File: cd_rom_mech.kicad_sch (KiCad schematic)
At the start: 182 parts, among them IC101 CXA1081, IC102 CXA1082BQ, IC107 RC4558, IC108 BA6290A, IC109 BA6290A, IC201 LC7881M, IC202 RC4558, IC203 RC4558, IC304 No Markings, Q608 BR 29

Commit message: Add more capacitor values, rearrange some schematics.
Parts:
- C105: value ~ -> 3.3uF 63V
- C105: value ? -> 22uF 6V
- C105: value ~ -> 22uF 6V
- C105: value ~ -> 470nF 25V
- C127: value ? -> 4.7uF 6V
- C138: value ? -> 470nF 25V
- C138: value 4.5nF -> 4.7nF
- VR101, VR103, VR104: value ~ -> 22K
- VR102: value ~ -> 15K
- VR105: value ~ -> 500
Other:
- moved on the sheet: C105, C127, C138, R105

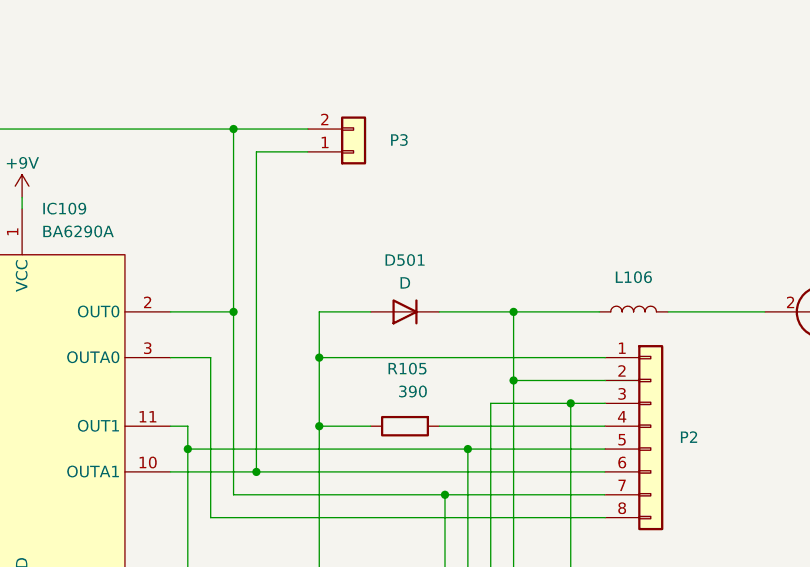
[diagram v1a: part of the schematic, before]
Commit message: Add markings for SMD Ds and Qs.
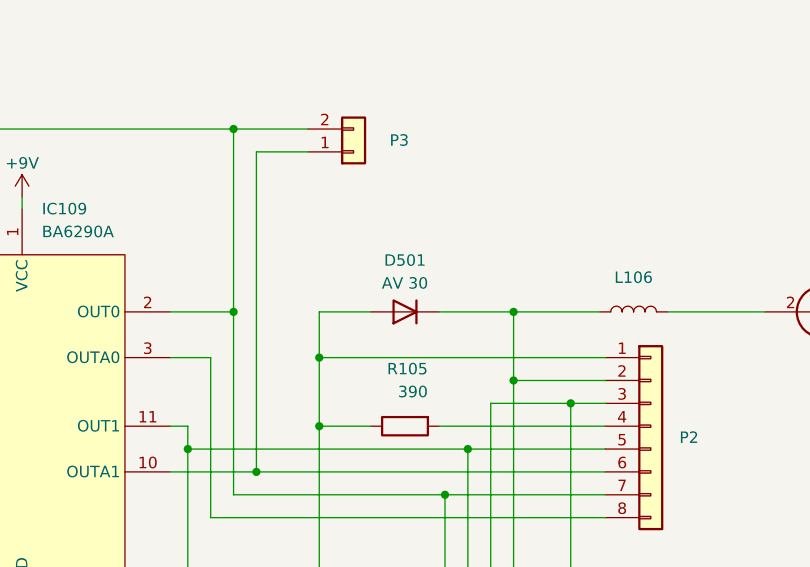
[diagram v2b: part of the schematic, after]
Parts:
- D501: value D -> AV 30
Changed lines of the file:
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@@
       (effects (font (size 1.27 1.27)))
     )
-    (property "Value" "D" (at 510.54 49.53 0)
+    (property "Value" "AV 30" (at 510.54 49.53 0)
       (effects (font (size 1.27 1.27)))
     )

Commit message: More schematic clean-up/annotation.
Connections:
- net PWR1 renamed +5VL
- no-connect marks 6 -> 7
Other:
- note added: "RF Amplifier for CD drive"
- note added: "Servo Signal Processor for CD drive"
- company: (none) -> By Cosam
- title: (none) -> PC Engine Duo CD-ROM Mech Interface
- moved on the sheet: C105, IC101, IC201, IC202A, IC202B, IC203A, IC203B, L106, P1, P5, Q608, R105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

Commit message: Correct some values/references.
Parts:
- R105: value 220K -> 270K
- R105: value 10M -> 1M
- R105: value 220K -> 240K
- R105: value 15K? -> 15K
- VR102: value 15K -> 22K
- VR105: value 500 -> 1K
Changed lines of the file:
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@@
       (effects (font (size 1.27 1.27)) (justify right))
     )
-    (property "Value" "15K" (at 149.225 379.095 0)
+    (property "Value" "22K" (at 149.225 379.095 0)
       (effects (font (size 1.27 1.27)) (justify right))
     )
@@
       (effects (font (size 1.27 1.27)))
     )
-    (property "Value" "220K" (at 159.385 147.955 0)
+    (property "Value" "270K" (at 159.385 147.955 0)
       (effects (font (size 1.27 1.27)))
     )
@@
       (effects (font (size 1.27 1.27)) (justify left))
     )
-    (property "Value" "10M" (at 563.88 259.08 0)
+    (property "Value" "1M" (at 563.88 259.08 0)
       (effects (font (size 1.27 1.27)) (justify left))
     )
@@
       (effects (font (size 1.27 1.27)) (justify right))
     )
-    (property "Value" "500" (at 201.295 379.095 0)
+    (property "Value" "1K" (at 201.295 379.095 0)
       (effects (font (size 1.27 1.27)) (justify right))
     )
@@
       (effects (font (size 1.27 1.27)))
     )
-    (property "Value" "220K" (at 194.31 365.76 90)
+    (property "Value" "240K" (at 194.31 365.76 90)
       (effects (font (size 1.27 1.27)))
     )
@@
       (effects (font (size 1.27 1.27)) (justify left))
     )
-    (property "Value" "15K?" (at 315.595 53.975 0)
+    (property "Value" "15K" (at 315.595 53.975 0)
       (effects (font (size 1.27 1.27)) (justify left))
     )
@@
       (effects (font (size 1.27 1.27)) (justify left))
     )
-    (property "Value" "10M" (at 563.88 289.56 0)
+    (property "Value" "1M" (at 563.88 289.56 0)
       (effects (font (size 1.27 1.27)) (justify left))
     )
@@
       (effects (font (size 1.27 1.27)) (justify right))
     )
-    (property "Value" "10M" (at 53.975 68.58 0)
+    (property "Value" "1M" (at 53.975 68.58 0)
       (effects (font (size 1.27 1.27)) (justify right))
     )

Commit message: Minor schematic/silkscreen changes.
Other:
- note added: "E/F Balance"
- note added: "Focus Bias"
- note added: "Focus Gain"
- note added: "Tracking Gain"
- note added: "VCO (PLL)"
- moved on the sheet: C105, C138, IC101, IC107A, IC107C, IC201, IC202A, IC202B, IC202C, IC203A, IC203B, IC203C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
